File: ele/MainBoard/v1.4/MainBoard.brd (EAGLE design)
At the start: 136.1 x 100 mm, 124 parts, among them IC1 MCP23017SP, IC2 74HC595D, IC3 74HC595D, X1 POWER_IN, X10 M7, X2 POWER_OUT, X3 M2, X4 M4, X5 M6, X6 M8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

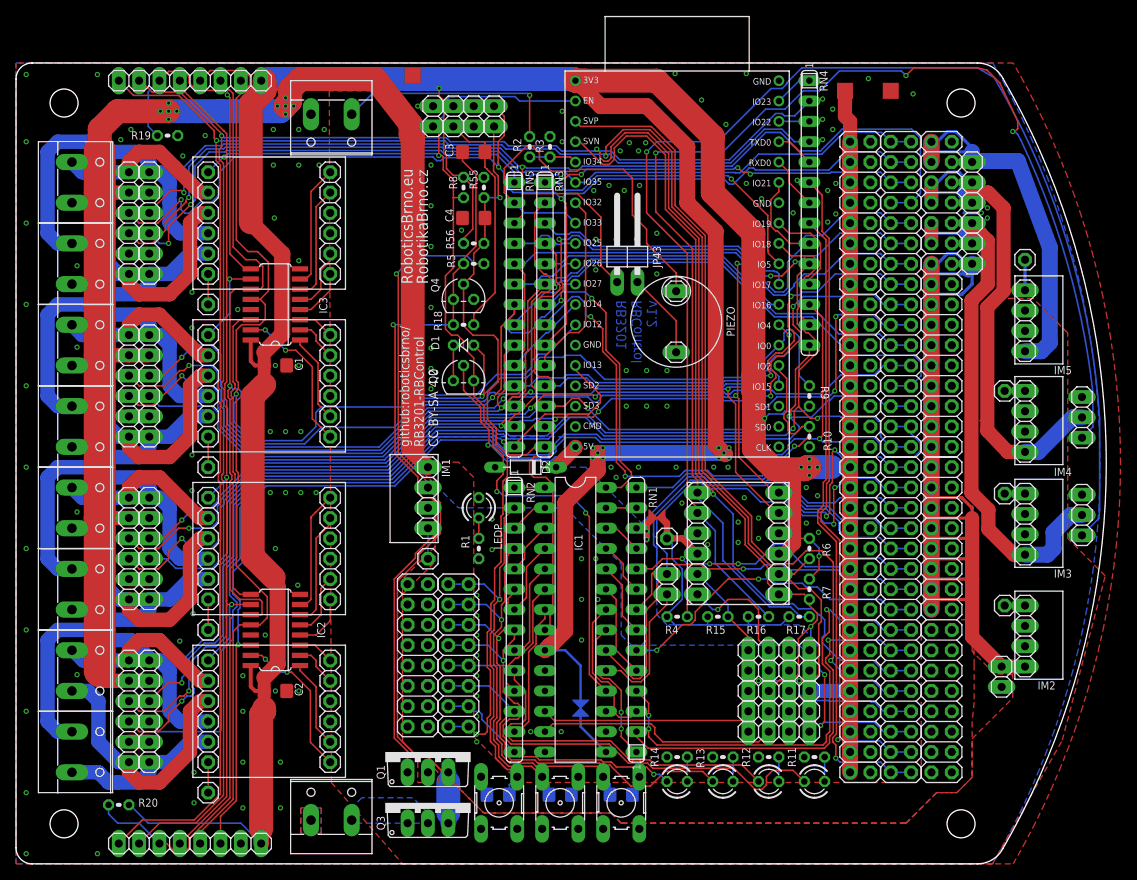
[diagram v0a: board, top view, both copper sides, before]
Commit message: ele: MainBoard - Add version v1.4 and restore version v1.2 after merge
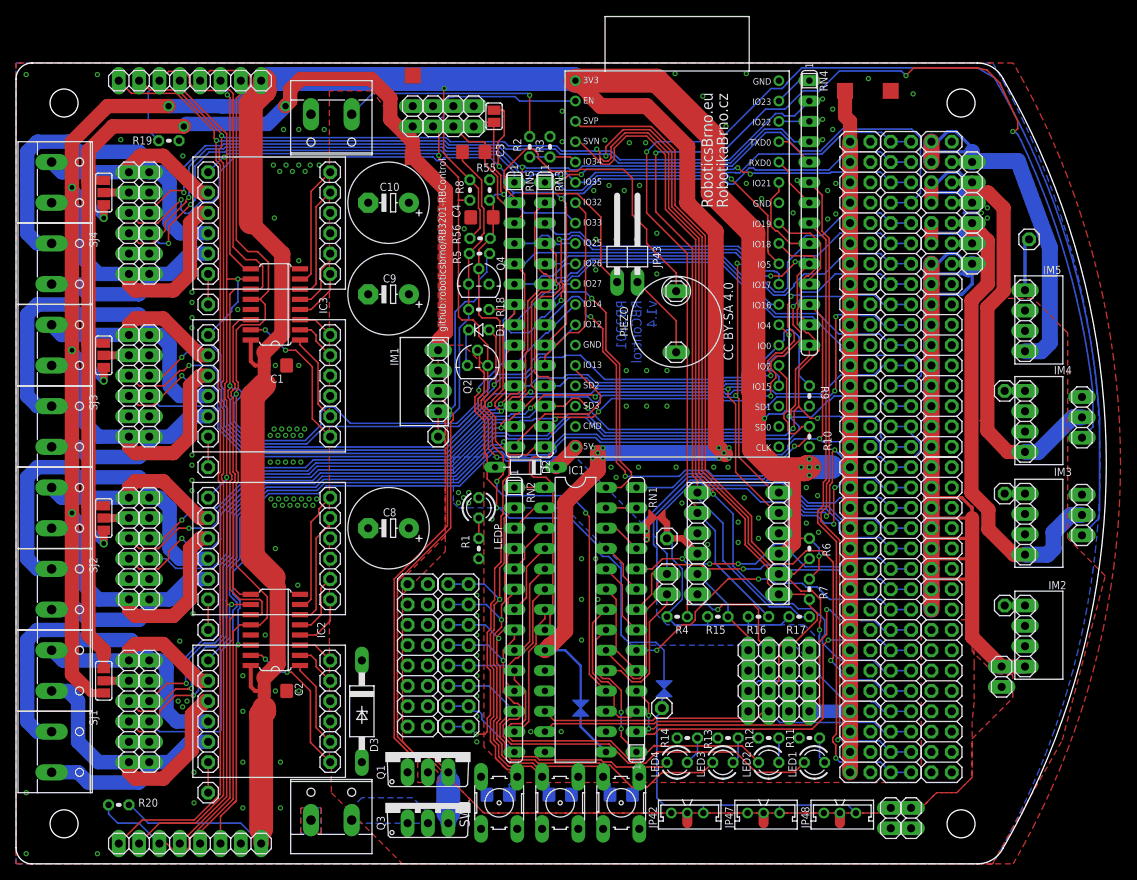
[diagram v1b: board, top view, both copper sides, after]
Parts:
- added C10, C8, C9: 16V/330uF, rcl:E5-10,5
- added D3: 1N5820, diode:F126Z12
- added JP46: 5V, pinhead:1X02
- added JP47, JP48: 292161-3, iServo_connector:292161-3
- added JP49: ISERVO, pinhead:1X01
- added JP50, JP51: VCC, pinhead:1X02
- added SJ1, SJ2, SJ3, SJ4: (no value), jumper:SJ_2
- added U$3: SJ_NC, SolderJumperNormallyClosed:SJ_NC
- C1, C2: value 100n -> 100n/16V
- C3, C4: value 10u -> 10u/16V
- C5, C6, C7: value 100n -> 100n/10V
- D1, D2: value (none) -> 1N4007
- JP24: device pinhead:1X02 -> jumper:SJ
- JP42: value I2C3_3V3 -> 292161-3; device pinhead:1X04 -> iServo_connector:292161-3
- Q1, Q3: value (none) -> IRF4905
- Q2, Q4: value (none) -> BS170
- moved JP42 19.1 mm to (83.8, 6.35)
- moved JP1 15.3 mm to (52.7, 53.3)
- moved IM1 14.7 mm to (54.0, 65.4)
- moved R14 2.70 mm to (83.8, 15.7)
- moved D1 2.69 mm to (57.8, 66.7)
- moved Q4 2.69 mm to (57.8, 72.4)
- moved R18 2.69 mm to (57.8, 69.2)
- moved JP5 2.59 mm to (126.5, 78.0)
- moved Q2 2.58 mm to (57.6, 62.2)
- moved X10 2.54 mm to (5.08, 74.9)
- moved X3 2.54 mm to (5.08, 24.1)
- moved X4 2.54 mm to (5.08, 44.5)
- moved X5 2.54 mm to (5.08, 64.8)
- moved X6 2.54 mm to (5.08, 85.1)
- moved X7 2.54 mm to (5.08, 14.0)
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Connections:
- new net ENC12PWR: JP31.2, JP35.2, SJ1.2
- new net ENC34PWR: JP32.2, JP36.2, SJ2.2
- new net ENC56PWR: JP33.2, JP37.2, SJ3.2
- new net ENC78PWR: JP34.2, JP38.2, SJ4.2
- new net ISERVO: JP42.3, JP47.3, JP48.3, JP49.1, U$3.P$2
- net +3V3: now also SJ1.1, SJ2.1, SJ3.1, SJ4.1; no longer JP42.4
- net +5V: now also JP46.1, SJ1.3, SJ2.3, SJ3.3, SJ4.3; no longer JP31.2, JP32.2, JP33.2, JP34.2, JP35.2, JP36.2, JP37.2, JP38.2
- net ENC8A: now also U$3.P$1
- net GND: now also C10.-, C8.-, C9.-, D3.A, JP42.1, JP46.2, JP47.1, JP48.1, JP50.2, JP51.2; no longer JP42.3
- net SCL: no longer JP42.1
- net SDA: no longer JP42.2
- net VCC: now also C10.+, C8.+, C9.+, D3.C, JP42.2, JP47.2, JP48.2, JP50.1, JP51.1
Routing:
- net +3V3: track 547.6 -> 661.1 mm, vias 19 -> 26
- net ENC8A: track 140.5 -> 221.2 mm, vias 3 -> 5
- net ISERVO: track 0.00 -> 41.0 mm
- net +5V: track 196.7 -> 156.2 mm, vias 12 -> 9
- net SDA: track 342.4 -> 331.4 mm, vias 5 -> 2
- net BAT_PROT: track 89.9 -> 80.6 mm
- net START_GATE: track 92.7 -> 84.0 mm
- net GND: track 9.91 -> 2.29 mm, vias 147 -> 156
- net ENC78PWR: track 0.00 -> 5.69 mm
- net ENC56PWR: track 0.00 -> 5.69 mm
- net ENC34PWR: track 0.00 -> 5.69 mm
- net ENC12PWR: track 0.00 -> 5.69 mm
- net EA1: track 58.3 -> 52.6 mm
- net SCL: track 338.9 -> 333.5 mm, vias 4 -> 3
- net 5V_2: track 168.6 -> 163.4 mm
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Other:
- board text added: "!"
- board text added: "(IO32/ENC8A)"
- board text added: "5V_2"
- board text added: "5V_3"
- board text added: "BLUE"
- board text added: "CC BY-SA 4.0"
- board text added: "GREEN"
- board text added: "IO14 \!5V"
- board text added: "IO15 \!S"
- board text added: "IO36 \!IN"
- board text added: "IO39 \!IN"
- board text added: "IO4 \!5V"
- board text added: "IO5 \!S"
- board text added: "PIEZZO"
- board text added: "RB3201"
- board text added: "RB3201 RBControl v1.4"
- board text added: "RB3201-RBControl v1.3"
- board text added: "RBControl"
- board text added: "RBControl RB3201 v1.4"
- board text added: "RED"
- board text added: "SW1"
- board text added: "SW2"
- board text added: "SW3"
- board text added: "UART"
- board text added: "YELLOW"
- board text added: "\!IN"
- board text added: "\!iS"
- board text added: "github:roboticsbrno/RB3201-RBControl"
- board text added: "iSERVO"
- board text added: "v1.4"
- board text removed: "C"
- board text removed: "D"
- board text removed: "IO15"
- board text removed: "IO5"
- board text removed: "LED1 RED EB3"
- board text removed: "LED2 YELLOW EB4"
- board text removed: "LED3 GREEN EB5"
- board text removed: "LED4 BLUE EB6"
- board text removed: "RB3201 RBControl v1.2"
- board text removed: "RB3201-RBControl v1.2"
- board text removed: "S1"
- board text removed: "S2"
- board text removed: "S3"
- board text removed: "github:roboticsbrno/ RB3201-RBControl CC BY-SA 4.0"
